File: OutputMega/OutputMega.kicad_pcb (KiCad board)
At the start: 2 copper layers, 78.7 x 92.1 mm, 143 parts, among them J1 Control JST5H, J10 Conn_02x13_Top_Bottom, J11 Ext Step Disable JST2H, J12 MegaProMiniR, J13 JTAG 2x05, J14 Dbg 2x03, J15 EStop Rly JST2H, J16 Sp Rly 1 JST2H, J17 Sp Rly 2 JST2H, J18 Step Disable JST2H, J19 EStop Sig0 JST2H, J2 EStop JST3H, J20 EStop Sig1 JST2H, J21 Conn_01x06_Male, J22 Conn_02x05_Odd_Even, J23 Pilot JST2H, J24 Sw 12v 1 JST2H, J25 Sw 12v 2 JST2H, J26 VFD Dir JST3H, J27 VFD Ctl JST3H, J3 EStop Rst JST2H, J4 TmrTest 1x03, J5 DbgPort JST4H, J6 RemPort JST3H, J7 12VIn JST2H, J8 PwrIn JST2H, J9 MegaProMiniL, K1 G6S-2, K2 G6S-2, K3 G6S-2, Q1 2N7002, Q10 2N7002, Q11 2N7002, Q12 2N7002, Q13 2N7002, Q2 2N7002, Q3 2N7002, Q4 2N7002, Q5 2N7002, Q6 2N7002, Q7 2N7002, Q8 2N7002, Q9 2N7002, U1 74HCT123, U10 MC34072AP, U11 LM4040DBZ-10, U2 74LS08, U3 LD1117S50TR_SOT223, U4 74LVC1G00, U5 74AUC2G34, U6 74AUC2G34, U7 74LVC2G157, U8 74LS08, U9 TLV9351

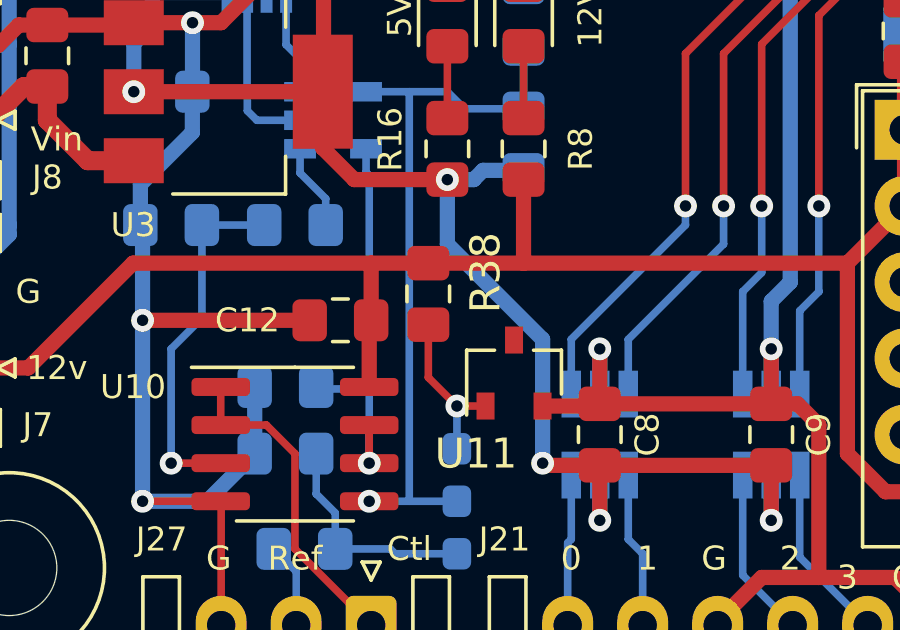
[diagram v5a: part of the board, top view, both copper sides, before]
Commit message: FT4232 Board and some fixes/
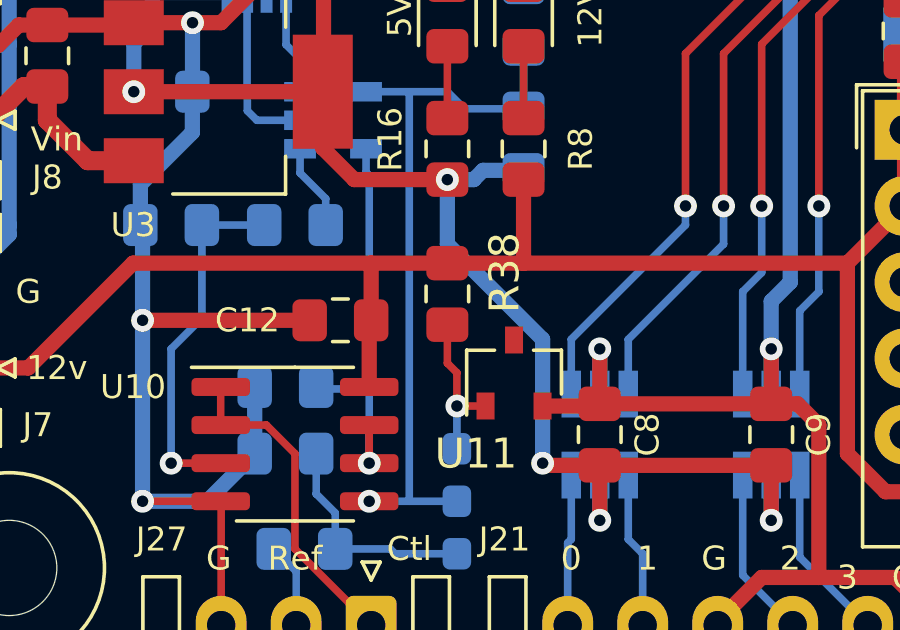
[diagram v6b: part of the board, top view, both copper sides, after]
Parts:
- moved R38 0.63 mm to (107.3, 141.4)
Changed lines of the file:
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@@
     (thickness 1.6)
     (drawings 68)
-    (tracks 1197)
+    (tracks 1198)
     (zones 0)
     (modules 143)
@@
   )
   (module Resistor_SMD:R_0805_2012Metric_Pad1.15x1.40mm_HandSolder (layer F.Cu)
-    (at 106.68 141.36 90)
+    (at 107.315 141.36 90)
     (descr "Resistor SMD 0805 (2012 Metric), square (rectangular) end terminal, IPC_7351 nominal with elongated pad for handsoldering. (Body size source: https://docs.google.com/spreadsheets/d/1BsfQQcO9C6DZCsRaXUlFlo91Tg2WpOkGARC1WS5S8t0/edit?usp=sharing), generated with kicad-footprint-generator")
     (tags "resistor handsolder")
@@
     (arrow2b (pts (xy 102.235 57.15) (xy 101.108496 57.736421)))
   )
-  (via (at 107.6325 145.0975) (size 0.762) (drill 0.381) (layers F.Cu B.Cu) (net 133))
   (segment (start 91.955 74.93) (end 90.805 73.78) (width 0.254) (layer F.Cu) (net 1))
   (segment (start 94.225 74.93) (end 91.955 74.93) (width 0.254) (layer F.Cu) (net 1))
@@
   (segment (start 123.095 134.08) (end 123.095 132.715) (width 0.508) (layer B.Cu) (net 69))
   (segment (start 104.71 144.4625) (end 104.71 142.305) (width 0.508) (layer F.Cu) (net 69))
-  (segment (start 104.775 140.335) (end 106.68 140.335) (width 0.508) (layer F.Cu) (net 69))
-  (segment (start 106.68 140.335) (end 109.855 140.335) (width 0.508) (layer F.Cu) (net 69))
+  (segment (start 104.775 140.335) (end 107.315 140.335) (width 0.508) (layer F.Cu) (net 69))
+  (segment (start 109.855 140.335) (end 107.315 140.335) (width 0.508) (layer F.Cu) (net 69))
   (segment (start 90.805 122.3175) (end 92.4725 122.3175) (width 0.254) (layer B.Cu) (net 70))
   (segment (start 92.71 122.555) (end 93.835 122.555) (width 0.254) (layer B.Cu) (net 70))
@@
   (segment (start 112.7125 128.27) (end 114.1525 129.71) (width 0.254) (layer B.Cu) (net 109))
   (segment (start 109.855 133.1775) (end 109.855 135.1915) (width 0.254) (layer B.Cu) (net 110))
+  (segment (start 104.775 148.3375) (end 104.71 148.2725) (width 0.254) (layer F.Cu) (net 110))
+  (segment (start 104.71 148.2725) (end 104.71 148.2725) (width 0.254) (layer F.Cu) (net 110))
+  (via (at 104.71 148.2725) (size 0.762) (drill 0.381) (layers F.Cu B.Cu) (net 110))
+  (segment (start 104.71 148.2725) (end 106.045 148.2725) (width 0.254) (layer B.Cu) (net 110))
+  (segment (start 104.6075 134.62) (end 104.605 134.6225) (width 0.254) (layer B.Cu) (net 110))
+  (segment (start 107.315 134.62) (end 104.6075 134.62) (width 0.254) (layer B.Cu) (net 110))
+  (segment (start 109.855 135.1915) (end 107.8865 135.1915) (width 0.254) (layer B.Cu) (net 110))
+  (segment (start 107.8865 135.1915) (end 107.315 134.62) (width 0.254) (layer B.Cu) (net 110))
+  (segment (start 106.045 148.2725) (end 106.045 134.62) (width 0.254) (layer B.Cu) (net 110))
+  (segment (start 107.315 148.2725) (end 107.6325 148.2725) (width 0.254) (layer B.Cu) (net 110))
+  (segment (start 106.045 148.2725) (end 107.315 148.2725) (width 0.254) (layer B.Cu) (net 110))
   (segment (start 103.3575 138.9675) (end 103.26 139.065) (width 0.254) (layer B.Cu) (net 111))
+  (segment (start 102.405 136.5225) (end 102.405 137.33) (width 0.254) (layer B.Cu) (net 111))
+  (segment (start 103.26 138.185) (end 103.26 139.065) (width 0.254) (layer B.Cu) (net 111))
+  (segment (start 102.405 137.33) (end 103.26 138.185) (width 0.254) (layer B.Cu) (net 111))
+  (segment (start 101.94 131.44) (end 101.94 133.055) (width 0.254) (layer B.Cu) (net 112))
+  (segment (start 102.405 133.52) (end 102.405 134.6225) (width 0.254) (layer B.Cu) (net 112))
+  (segment (start 101.94 133.055) (end 102.405 133.52) (width 0.254) (layer B.Cu) (net 112))
   (segment (start 160.8775 144.78) (end 160.9725 144.875) (width 0.254) (layer B.Cu) (net 113))
   (segment (start 158.8975 144.78) (end 160.8775 144.78) (width 0.254) (layer B.Cu) (net 113))
@@
   (segment (start 160.825 119.3825) (end 160.825 118.745) (width 0.254) (layer B.Cu) (net 130))
   (segment (start 160.825 118.745) (end 160.7275 118.6475) (width 0.254) (layer B.Cu) (net 130))
-  (segment (start 104.775 148.3375) (end 104.71 148.2725) (width 0.254) (layer F.Cu) (net 110))
-  (segment (start 104.71 148.2725) (end 104.71 148.2725) (width 0.254) (layer F.Cu) (net 110))
-  (via (at 104.71 148.2725) (size 0.762) (drill 0.381) (layers F.Cu B.Cu) (net 110))
-  (segment (start 104.71 148.2725) (end 106.045 148.2725) (width 0.254) (layer B.Cu) (net 110))
-  (segment (start 104.6075 134.62) (end 104.605 134.6225) (width 0.254) (layer B.Cu) (net 110))
-  (segment (start 107.315 134.62) (end 104.6075 134.62) (width 0.254) (layer B.Cu) (net 110))
-  (segment (start 109.855 135.1915) (end 107.8865 135.1915) (width 0.254) (layer B.Cu) (net 110))
-  (segment (start 107.8865 135.1915) (end 107.315 134.62) (width 0.254) (layer B.Cu) (net 110))
-  (segment (start 106.045 148.2725) (end 106.045 134.62) (width 0.254) (layer B.Cu) (net 110))
-  (segment (start 107.315 148.2725) (end 107.6325 148.2725) (width 0.254) (layer B.Cu) (net 110))
-  (segment (start 106.045 148.2725) (end 107.315 148.2725) (width 0.254) (layer B.Cu) (net 110))
-  (segment (start 102.405 136.5225) (end 102.405 137.33) (width 0.254) (layer B.Cu) (net 111))
-  (segment (start 103.26 138.185) (end 103.26 139.065) (width 0.254) (layer B.Cu) (net 111))
-  (segment (start 102.405 137.33) (end 103.26 138.185) (width 0.254) (layer B.Cu) (net 111))
-  (segment (start 101.94 131.44) (end 101.94 133.055) (width 0.254) (layer B.Cu) (net 112))
-  (segment (start 102.405 133.52) (end 102.405 134.6225) (width 0.254) (layer B.Cu) (net 112))
-  (segment (start 101.94 133.055) (end 102.405 133.52) (width 0.254) (layer B.Cu) (net 112))
   (segment (start 103.5775 149.86) (end 103.5775 148.6625) (width 0.254) (layer B.Cu) (net 131))
   (segment (start 102.9425 148.0275) (end 102.9425 146.685) (width 0.254) (layer B.Cu) (net 131))
@@
   (segment (start 102.275 150.6075) (end 101.5275 149.86) (width 0.254) (layer B.Cu) (net 132))
   (segment (start 102.275 152.4) (end 102.275 150.6075) (width 0.254) (layer B.Cu) (net 132))
-  (segment (start 106.68 144.145) (end 107.6325 145.0975) (width 0.254) (layer F.Cu) (net 133))
-  (segment (start 106.68 142.385) (end 106.68 144.145) (width 0.254) (layer F.Cu) (net 133))
+  (via (at 107.6325 145.0975) (size 0.762) (drill 0.381) (layers F.Cu B.Cu) (net 133))
   (segment (start 107.6325 145.0975) (end 108.5875 145.0975) (width 0.254) (layer F.Cu) (net 133))
   (segment (start 107.6325 146.5225) (end 107.6325 145.0975) (width 0.254) (layer B.Cu) (net 133))
+  (segment (start 107.315 143.66875) (end 107.315 142.385) (width 0.254) (layer F.Cu) (net 133))
+  (segment (start 107.6325 145.0975) (end 107.6325 143.98625) (width 0.254) (layer F.Cu) (net 133))
+  (segment (start 107.6325 143.98625) (end 107.315 143.66875) (width 0.254) (layer F.Cu) (net 133))
 )

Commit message: Updates for new boards.
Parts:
- C6: value C -> 10uf
- R16, R22: value R -> 7.5k
- R18, R19, R20, R21, R34, R35, R36, R37, R8: value R -> 24k
- R23: value R -> 2.4k
- R26, R27, R28, R29: value R -> 10k
- R32: value R -> 750
- R38: value R -> 1k
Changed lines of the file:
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@@
     (add_net /WDR)
     (add_net /WDRC)
+    (add_net "Net-(D4-Pad1)")
+    (add_net "Net-(D9-Pad1)")
+    (add_net "Net-(J12-Pad55)")
+    (add_net "Net-(J12-Pad61)")
+    (add_net "Net-(J12-Pad62)")
+    (add_net "Net-(J12-Pad64)")
+    (add_net "Net-(J12-Pad66)")
+    (add_net "Net-(J12-Pad68)")
+    (add_net "Net-(J12-Pad73)")
+    (add_net "Net-(J12-Pad74)")
+    (add_net "Net-(J13-Pad7)")
+    (add_net "Net-(J13-Pad8)")
+    (add_net "Net-(J22-Pad9)")
+    (add_net "Net-(J9-Pad1)")
+    (add_net "Net-(J9-Pad2)")
+    (add_net "Net-(J9-Pad21)")
+    (add_net "Net-(J9-Pad8)")
+    (add_net "Net-(K1-Pad10)")
+    (add_net "Net-(K1-Pad3)")
+    (add_net "Net-(K2-Pad10)")
+    (add_net "Net-(K2-Pad3)")
+    (add_net "Net-(K2-Pad8)")
+    (add_net "Net-(K2-Pad9)")
+    (add_net "Net-(K3-Pad10)")
+    (add_net "Net-(K3-Pad3)")
+    (add_net "Net-(K3-Pad4)")
+    (add_net "Net-(K3-Pad5)")
+    (add_net "Net-(U1-Pad10)")
+    (add_net "Net-(U1-Pad12)")
+    (add_net "Net-(U1-Pad5)")
+    (add_net "Net-(U1-Pad6)")
+    (add_net "Net-(U1-Pad7)")
+    (add_net "Net-(U1-Pad9)")
+    (add_net "Net-(U7-Pad3)")
   )
   (net_class Power ""
@@
       (effects (font (size 1 1) (thickness 0.15)))
     )
-    (fp_text value R (at 0 1.65 90) (layer F.Fab)
+    (fp_text value 1k (at 0 1.65 90) (layer F.Fab)
       (effects (font (size 1 1) (thickness 0.15)))
     )
@@
       (effects (font (size 0.8 0.8) (thickness 0.12)))
     )
-    (fp_text value R (at 0 1.65) (layer F.Fab)
+    (fp_text value 750 (at 0 1.65) (layer F.Fab)
       (effects (font (size 1 1) (thickness 0.15)))
     )
@@
       (effects (font (size 0.8 0.8) (thickness 0.12)))
     )
-    (fp_text value R (at 0 1.65 90) (layer F.Fab)
+    (fp_text value 24k (at 0 1.65 90) (layer F.Fab)
       (effects (font (size 1 1) (thickness 0.15)))
     )
@@
       (effects (font (size 0.8 0.8) (thickness 0.12)))
     )
-    (fp_text value R (at 0 1.65 90) (layer F.Fab)
+    (fp_text value 24k (at 0 1.65 90) (layer F.Fab)
       (effects (font (size 1 1) (thickness 0.15)))
     )
@@
       (effects (font (size 0.8 0.8) (thickness 0.12)))
     )
-    (fp_text value R (at 0 1.65) (layer F.Fab)
+    (fp_text value 24k (at 0 1.65) (layer F.Fab)
       (effects (font (size 1 1) (thickness 0.15)))
     )
@@
       (effects (font (size 0.8 0.8) (thickness 0.12)))
     )
-    (fp_text value R (at 0 1.65) (layer F.Fab)
+    (fp_text value 24k (at 0 1.65) (layer F.Fab)
       (effects (font (size 1 1) (thickness 0.15)))
     )
@@
       (effects (font (size 1 1) (thickness 0.15)) (justify mirror))
     )
-    (fp_text value R (at 0 -1.65) (layer B.Fab)
+    (fp_text value 10k (at 0 -1.65) (layer B.Fab)
       (effects (font (size 1 1) (thickness 0.15)) (justify mirror))
     )
@@
       (effects (font (size 1 1) (thickness 0.15)) (justify mirror))
     )
-    (fp_text value R (at 0 -1.65) (layer B.Fab)
+    (fp_text value 10k (at 0 -1.65) (layer B.Fab)
       (effects (font (size 1 1) (thickness 0.15)) (justify mirror))
     )
@@
       (effects (font (size 1 1) (thickness 0.15)) (justify mirror))
     )
-    (fp_text value R (at 0 -1.65) (layer B.Fab)
+    (fp_text value 10k (at 0 -1.65) (layer B.Fab)
       (effects (font (size 1 1) (thickness 0.15)) (justify mirror))
     )
@@
       (effects (font (size 1 1) (thickness 0.15)) (justify mirror))
     )
-    (fp_text value R (at 0 -1.65) (layer B.Fab)
+    (fp_text value 10k (at 0 -1.65) (layer B.Fab)
       (effects (font (size 1 1) (thickness 0.15)) (justify mirror))
     )
@@
       (effects (font (size 1 1) (thickness 0.15)) (justify mirror))
     )
-    (fp_text value R (at 0 -1.65) (layer B.Fab)
+    (fp_text value 2.4k (at 0 -1.65) (layer B.Fab)
       (effects (font (size 1 1) (thickness 0.15)) (justify mirror))
     )
@@
       (effects (font (size 0.8 0.8) (thickness 0.12)))
     )
-    (fp_text value R (at 0 1.65) (layer F.Fab)
+    (fp_text value 7.5k (at 0 1.65) (layer F.Fab)
       (effects (font (size 1 1) (thickness 0.15)))
     )
@@
       (effects (font (size 0.8 0.8) (thickness 0.12)))
     )
-    (fp_text value R (at 0 1.65) (layer F.Fab)
+    (fp_text value 24k (at 0 1.65) (layer F.Fab)
       (effects (font (size 1 1) (thickness 0.15)))
     )
@@
       (effects (font (size 0.8 0.8) (thickness 0.12)))
     )
-    (fp_text value R (at 0 1.65) (layer F.Fab)
+    (fp_text value 24k (at 0 1.65) (layer F.Fab)
       (effects (font (size 1 1) (thickness 0.15)))
     )
@@
       (effects (font (size 0.8 0.8) (thickness 0.12)))
     )
-    (fp_text value R (at 0 1.65) (layer F.Fab)
+    (fp_text value 24k (at 0 1.65) (layer F.Fab)
       (effects (font (size 1 1) (thickness 0.15)))
     )
@@
       (effects (font (size 0.8 0.8) (thickness 0.12)))
     )
-    (fp_text value R (at 0 1.65 90) (layer F.Fab)
+    (fp_text value 24k (at 0 1.65 90) (layer F.Fab)
       (effects (font (size 1 1) (thickness 0.15)))
     )
@@
       (effects (font (size 0.8 0.8) (thickness 0.12)))
     )
-    (fp_text value R (at 0 1.65 90) (layer F.Fab)
+    (fp_text value 7.5k (at 0 1.65 90) (layer F.Fab)
       (effects (font (size 1 1) (thickness 0.15)))
     )
@@
       (effects (font (size 0.8 0.8) (thickness 0.12)))
     )
-    (fp_text value R (at 0 1.65 90) (layer F.Fab)
+    (fp_text value 24k (at 0 1.65 90) (layer F.Fab)
       (effects (font (size 1 1) (thickness 0.15)))
     )
@@
       (effects (font (size 0.8 0.8) (thickness 0.12)))
     )
-    (fp_text value C (at 0 1.65) (layer F.Fab)
+    (fp_text value 10uf (at 0 1.65) (layer F.Fab)
       (effects (font (size 1 1) (thickness 0.15)))
     )
